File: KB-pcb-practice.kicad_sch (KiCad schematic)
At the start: 56 parts, among them J1 Conn_01x03, SW1 Reset, SW2 Boot, U1 RP2040, U2 IS31FL3742A-QFLS4-TR, U3 W25Q128JVS, U4 IS31FL3742A-QFLS4-TR, U5 NCP1117-3.3_SOT223, Y1 ABLS-12.000MHZ-B4-T

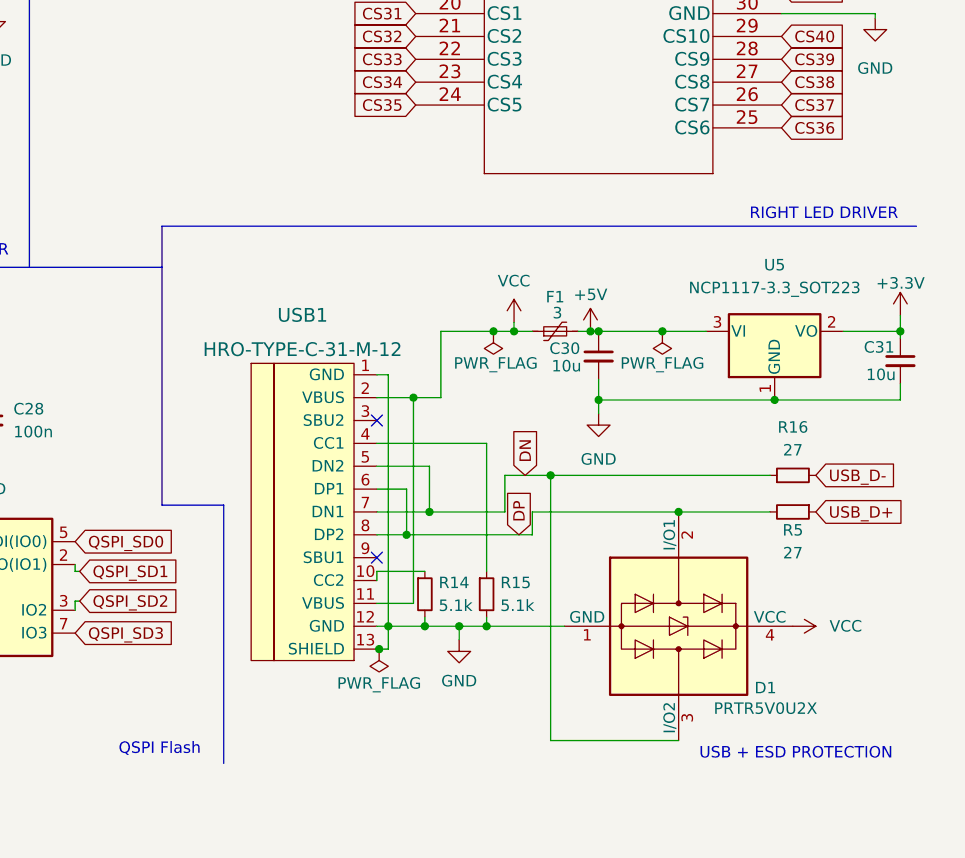
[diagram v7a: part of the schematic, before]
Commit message: Added fill zones  and some art to PCB
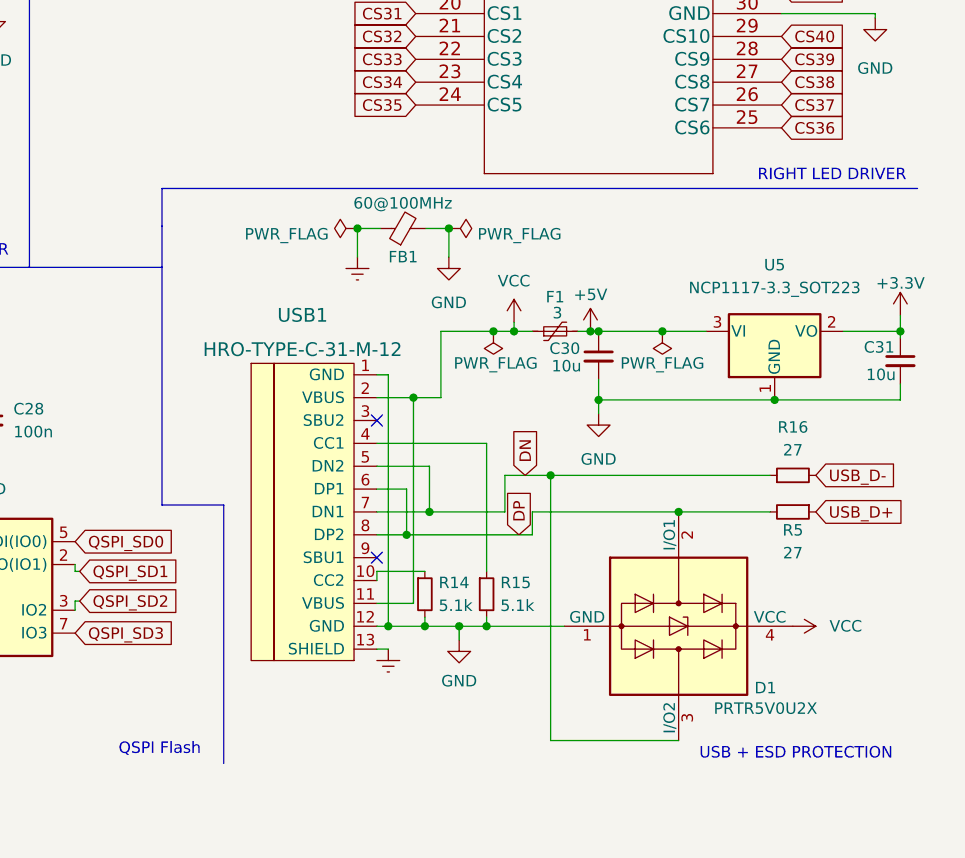
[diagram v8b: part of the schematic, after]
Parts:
- added FB1: 60@100MHz, Inductor_SMD:L_0805_2012Metric_Pad1.15x1.40mm_HandSolder, symbol Device:FerriteBead_Small
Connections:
- net GND: now also FB1.2; no longer USB1.13 (SHIELD)
- new net Earth: FB1.1, USB1.13 (SHIELD)
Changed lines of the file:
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@@
   (junction (at 73.025 169.545) (diameter 0) (color 0 0 0 0)
   )
+  (junction (at 233.045 106.68) (diameter 0) (color 0 0 0 0)
+  )
   (junction (at 204.724 60.706) (diameter 0) (color 0 0 0 0)
   )
@@
   (junction (at 229.362 62.484) (diameter 0) (color 0 0 0 0)
   )
+  (junction (at 222.885 106.68) (diameter 0) (color 0 0 0 0)
+  )
   (junction (at 230.378 150.876) (diameter 0) (color 0 0 0 0)
   )
@@
   (junction (at 248.7778 118.11) (diameter 0) (color 0 0 0 0)
   )
-  (junction (at 225.298 153.416) (diameter 0) (color 0 0 0 0)
-  )
   (no_connect (at 225.044 143.256))
   (no_connect (at 225.044 128.016))
@@
     (stroke (width 0) (type default))
   )
+  (wire (pts (xy 233.045 106.68) (xy 233.045 109.855))
+    (stroke (width 0) (type default))
+  )
   (wire (pts (xy 230.378 149.86) (xy 230.378 150.876))
     (stroke (width 0) (type default))
@@
     (stroke (width 0) (type default))
   )
-  (polyline (pts (xy 201.168 106.426) (xy 284.988 106.426))
-    (stroke (width 0) (type default))
-  )
   (wire (pts (xy 116.5589 135.5942) (xy 116.5589 135.4395))
     (stroke (width 0) (type default))
@@
     (stroke (width 0) (type default))
   )
+  (wire (pts (xy 230.505 106.68) (xy 233.045 106.68))
+    (stroke (width 0) (type default))
+  )
   (wire (pts (xy 25.908 188.214) (xy 35.306 188.214))
     (stroke (width 0) (type default))
@@
     (stroke (width 0) (type default))
   )
-  (wire (pts (xy 226.314 153.416) (xy 226.314 150.876))
-    (stroke (width 0) (type default))
-  )
   (wire (pts (xy 49.022 161.036) (xy 53.848 161.036))
     (stroke (width 0) (type default))
@@
     (stroke (width 0) (type default))
   )
-  (wire (pts (xy 225.298 153.416) (xy 226.314 153.416))
+  (wire (pts (xy 225.044 153.416) (xy 226.314 153.416))
     (stroke (width 0) (type default))
   )
@@
     (stroke (width 0) (type default))
   )
-  (wire (pts (xy 225.044 153.416) (xy 225.298 153.416))
-    (stroke (width 0) (type default))
-  )
   (wire (pts (xy 200.66 42.164) (xy 206.502 42.164))
     (stroke (width 0) (type default))
@@
     (stroke (width 0) (type default))
   )
+  (polyline (pts (xy 201.1715 102.235) (xy 201.1715 106.4126))
+    (stroke (width 0) (type default))
+  )
   (wire (pts (xy 25.908 53.594) (xy 25.146 53.594))
     (stroke (width 0) (type default))
@@
     (stroke (width 0) (type default))
   )
+  (polyline (pts (xy 201.1715 102.235) (xy 285.115 102.235))
+    (stroke (width 0) (type default))
+  )
   (wire (pts (xy 53.848 169.672) (xy 63.754 169.672))
     (stroke (width 0) (type default))
@@
     (stroke (width 0) (type default))
   )
+  (wire (pts (xy 225.425 106.68) (xy 222.885 106.68))
+    (stroke (width 0) (type default))
+  )
   (wire (pts (xy 116.5589 133.1469) (xy 116.5589 132.8995))
     (stroke (width 0) (type default))
@@
     (stroke (width 0) (type default))
   )
+  (wire (pts (xy 222.885 106.68) (xy 222.885 109.855))
+    (stroke (width 0) (type default))
+  )
   (wire (pts (xy 256.7688 118.11) (xy 261.62 118.11))
     (stroke (width 0) (type default))
@@
     (effects (font (size 1.27 1.27)) (justify left bottom))
   )
-  (text "RIGHT LED DRIVER" (at 266.446 105.918 0)
+  (text "RIGHT LED DRIVER" (at 267.335 101.6 0)
     (effects (font (size 1.27 1.27)) (justify left bottom))
   )
@@
     )
   )
+  (symbol (lib_id "power:Earth") (at 222.885 109.855 0) (unit 1)
+    (in_bom yes) (on_board yes) (dnp no) (fields_autoplaced)
+    (property "Reference" "#PWR095" (at 222.885 116.205 0)
+      (effects (font (size 1.27 1.27)) hide)
+    )
+    (property "Value" "Earth" (at 222.885 113.665 0)
+      (effects (font (size 1.27 1.27)) hide)
+    )
+    (property "Footprint" "" (at 222.885 109.855 0)
+      (effects (font (size 1.27 1.27)) hide)
+    )
+    (property "Datasheet" "~" (at 222.885 109.855 0)
+      (effects (font (size 1.27 1.27)) hide)
+    )
+    (pin "1")
+    (instances
+      (project "KB-pcb-practice"
+        (path "/806fdcd7-25b2-4878-addb-1faa319c0ab0"
+          (reference "#PWR095") (unit 1)
+        )
+      )
+    )
+  )
   (symbol (lib_id "power:+5V") (at 109.474 175.514 0) (unit 1)
     (in_bom yes) (on_board yes) (dnp no)
@@
     )
   )
+  (symbol (lib_id "power:Earth") (at 226.314 153.416 0) (unit 1)
+    (in_bom yes) (on_board yes) (dnp no) (fields_autoplaced)
+    (property "Reference" "#PWR094" (at 226.314 159.766 0)
+      (effects (font (size 1.27 1.27)) hide)
+    )
+    (property "Value" "Earth" (at 226.314 157.226 0)
+      (effects (font (size 1.27 1.27)) hide)
+    )
+    (property "Footprint" "" (at 226.314 153.416 0)
+      (effects (font (size 1.27 1.27)) hide)
+    )
+    (property "Datasheet" "~" (at 226.314 153.416 0)
+      (effects (font (size 1.27 1.27)) hide)
+    )
+    (pin "1")
+    (instances
+      (project "KB-pcb-practice"
+        (path "/806fdcd7-25b2-4878-addb-1faa319c0ab0"
+          (reference "#PWR094") (unit 1)
+        )
+      )
+    )
+  )
   (symbol (lib_id "ul_IS31FL3742A-QFLS4-TR_custom:IS31FL3742A-QFLS4-TR") (at 131.445 33.655 0) (unit 1)
     (in_bom yes) (on_board yes) (dnp no) (fields_autoplaced)
@@
     )
   )
+  (symbol (lib_id "Device:FerriteBead_Small") (at 227.965 106.68 90) (unit 1)
+    (in_bom yes) (on_board yes) (dnp no)
+    (property "Reference" "FB1" (at 227.965 109.855 90)
+      (effects (font (size 1.27 1.27)))
+    )
+    (property "Value" "60@100MHz" (at 227.9269 103.881 90)
+      (effects (font (size 1.27 1.27)))
+    )
+    (property "Footprint" "Inductor_SMD:L_0805_2012Metric_Pad1.15x1.40mm_HandSolder" (at 227.965 108.458 90)
+      (effects (font (size 1.27 1.27)) hide)
+    )
+    (property "Datasheet" "~" (at 227.965 106.68 0)
+      (effects (font (size 1.27 1.27)) hide)
+    )
+    (pin "1")
+    (pin "2")
+    (instances
+      (project "KB-pcb-practice"
+        (path "/806fdcd7-25b2-4878-addb-1faa319c0ab0"
+          (reference "FB1") (unit 1)
+        )
+      )
+    )
+  )
   (symbol (lib_id "Device:R_Small") (at 155.194 144.018 90) (unit 1)
     (in_bom yes) (on_board yes) (dnp no) (fields_autoplaced)
@@
     )
   )
+  (symbol (lib_id "power:GND") (at 233.045 109.855 0) (unit 1)
+    (in_bom yes) (on_board yes) (dnp no) (fields_autoplaced)
+    (property "Reference" "#PWR096" (at 233.045 116.205 0)
+      (effects (font (size 1.27 1.27)) hide)
+    )
+    (property "Value" "GND" (at 233.045 114.935 0)
+      (effects (font (size 1.27 1.27)))
+    )
+    (property "Footprint" "" (at 233.045 109.855 0)
+      (effects (font (size 1.27 1.27)) hide)
+    )
+    (property "Datasheet" "" (at 233.045 109.855 0)
+      (effects (font (size 1.27 1.27)) hide)
+    )
+    (pin "1")
+    (instances
+      (project "KB-pcb-practice"
+        (path "/806fdcd7-25b2-4878-addb-1faa319c0ab0"
+          (reference "#PWR096") (unit 1)
+        )
+      )
+    )
+  )
   (symbol (lib_id "Device:C_Small") (at 35.306 184.404 0) (unit 1)
     (in_bom yes) (on_board yes) (dnp no) (fields_autoplaced)
@@
     )
   )
+  (symbol (lib_id "power:PWR_FLAG") (at 233.045 106.68 270) (unit 1)
+    (in_bom yes) (on_board yes) (dnp no) (fields_autoplaced)
+    (property "Reference" "#FLG02" (at 234.95 106.68 0)
+      (effects (font (size 1.27 1.27)) hide)
+    )
+    (property "Value" "PWR_FLAG" (at 236.22 107.315 90)
+      (effects (font (size 1.27 1.27)) (justify left))
+    )
+    (property "Footprint" "" (at 233.045 106.68 0)
+      (effects (font (size 1.27 1.27)) hide)
+    )
+    (property "Datasheet" "~" (at 233.045 106.68 0)
+      (effects (font (size 1.27 1.27)) hide)
+    )
+    (pin "1")
+    (instances
+      (project "KB-pcb-practice"
+        (path "/806fdcd7-25b2-4878-addb-1faa319c0ab0"
+          (reference "#FLG02") (unit 1)
+        )
+      )
+    )
+  )
   (symbol (lib_id "power:GND") (at 182.499 82.423 0) (unit 1)
     (in_bom yes) (on_board yes) (dnp no) (fields_autoplaced)
@@
     )
   )
+  (symbol (lib_id "power:PWR_FLAG") (at 222.885 106.68 90) (unit 1)
+    (in_bom yes) (on_board yes) (dnp no) (fields_autoplaced)
+    (property "Reference" "#FLG01" (at 220.98 106.68 0)
+      (effects (font (size 1.27 1.27)) hide)
+    )
+    (property "Value" "PWR_FLAG" (at 219.71 107.315 90)
+      (effects (font (size 1.27 1.27)) (justify left))
+    )
+    (property "Footprint" "" (at 222.885 106.68 0)
+      (effects (font (size 1.27 1.27)) hide)
+    )
+    (property "Datasheet" "~" (at 222.885 106.68 0)
+      (effects (font (size 1.27 1.27)) hide)
+    )
+    (pin "1")
+    (instances
+      (project "KB-pcb-practice"
+        (path "/806fdcd7-25b2-4878-addb-1faa319c0ab0"
+          (reference "#FLG01") (unit 1)
+        )
+      )
+    )
+  )
   (symbol (lib_id "power:GND") (at 279.908 35.814 0) (mirror y) (unit 1)
     (in_bom yes) (on_board yes) (dnp no)
@@
         )
       )
-    )
-  )
-  (symbol (lib_id "power:PWR_FLAG") (at 225.298 153.416 180) (unit 1)
-    (in_bom yes) (on_board yes) (dnp no)
-    (property "Reference" "#FLG0104" (at 225.298 155.321 0)
-      (effects (font (size 1.27 1.27)) hide)
-    )
-    (property "Value" "PWR_FLAG" (at 225.298 157.226 0)
-      (effects (font (size 1.27 1.27)))
-    )
-    (property "Footprint" "" (at 225.298 153.416 0)
-      (effects (font (size 1.27 1.27)) hide)
-    )
-    (property "Datasheet" "~" (at 225.298 153.416 0)
-      (effects (font (size 1.27 1.27)) hide)
-    )
-    (pin "1")
-    (instances
-      (project "KB-pcb-practice"
-        (path "/806fdcd7-25b2-4878-addb-1faa319c0ab0"
-          (reference "#FLG0104") (unit 1)
-        )
-      )
